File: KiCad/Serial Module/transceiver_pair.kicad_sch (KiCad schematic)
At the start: 22 parts, among them U10 74LVC125, U11 THVD1420D, U12 THVD1420D, U9 74LVC125

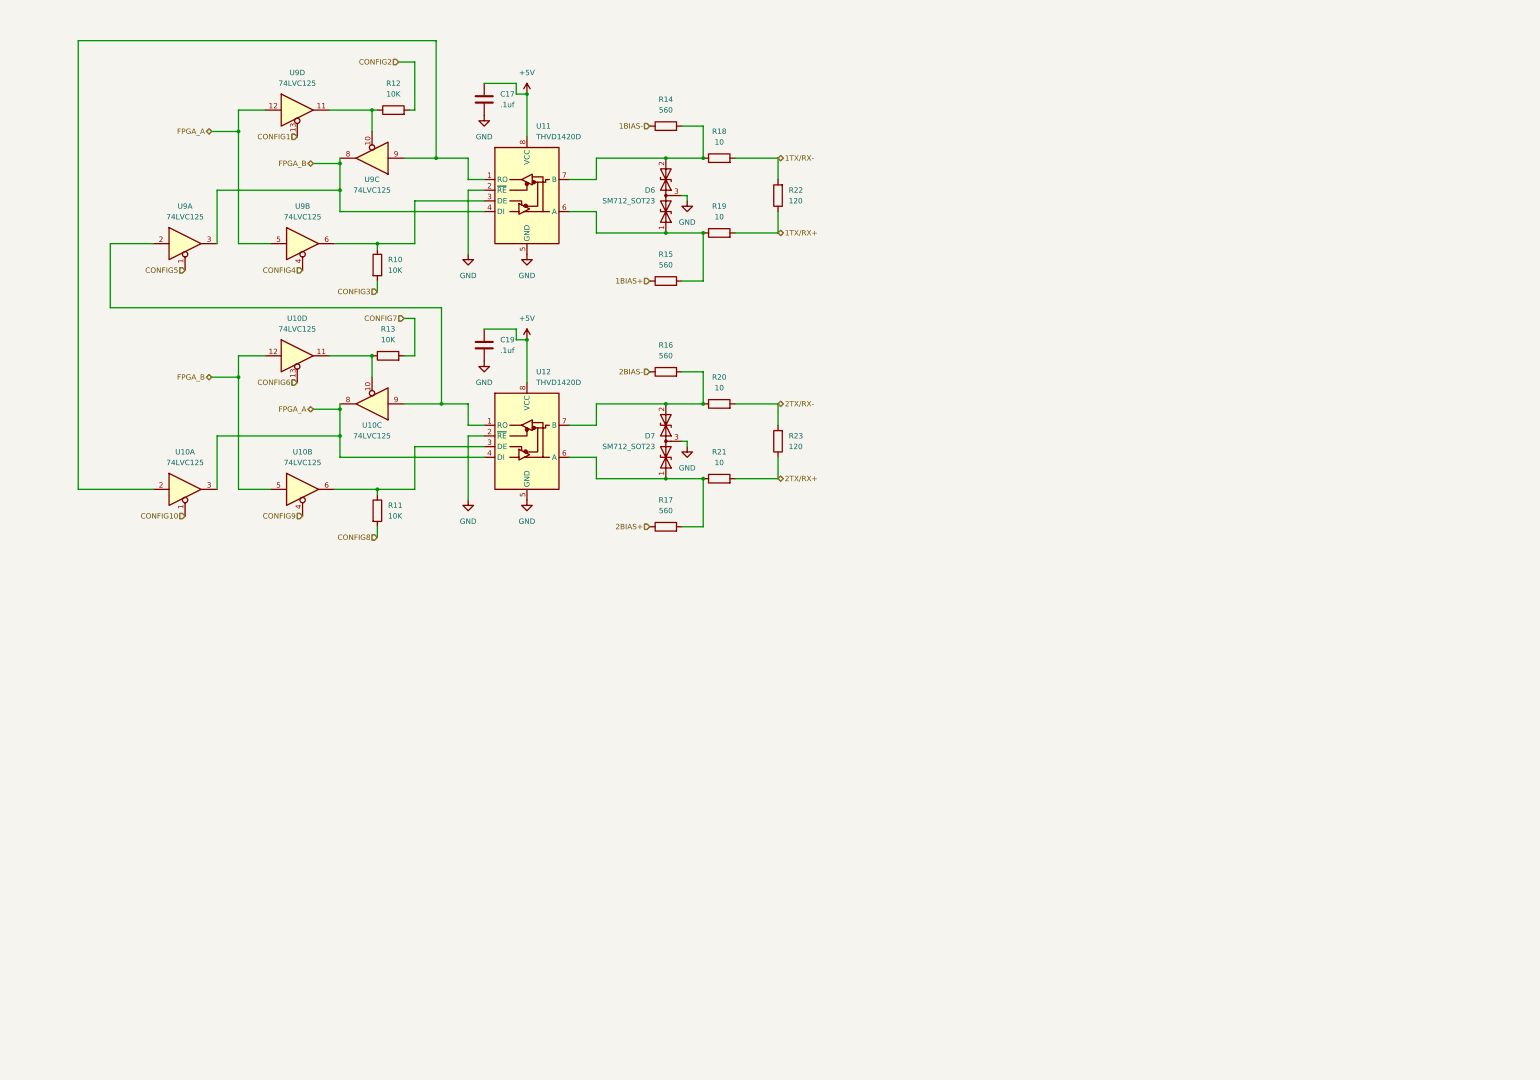
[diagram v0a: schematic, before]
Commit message: update serial module and backplane hw
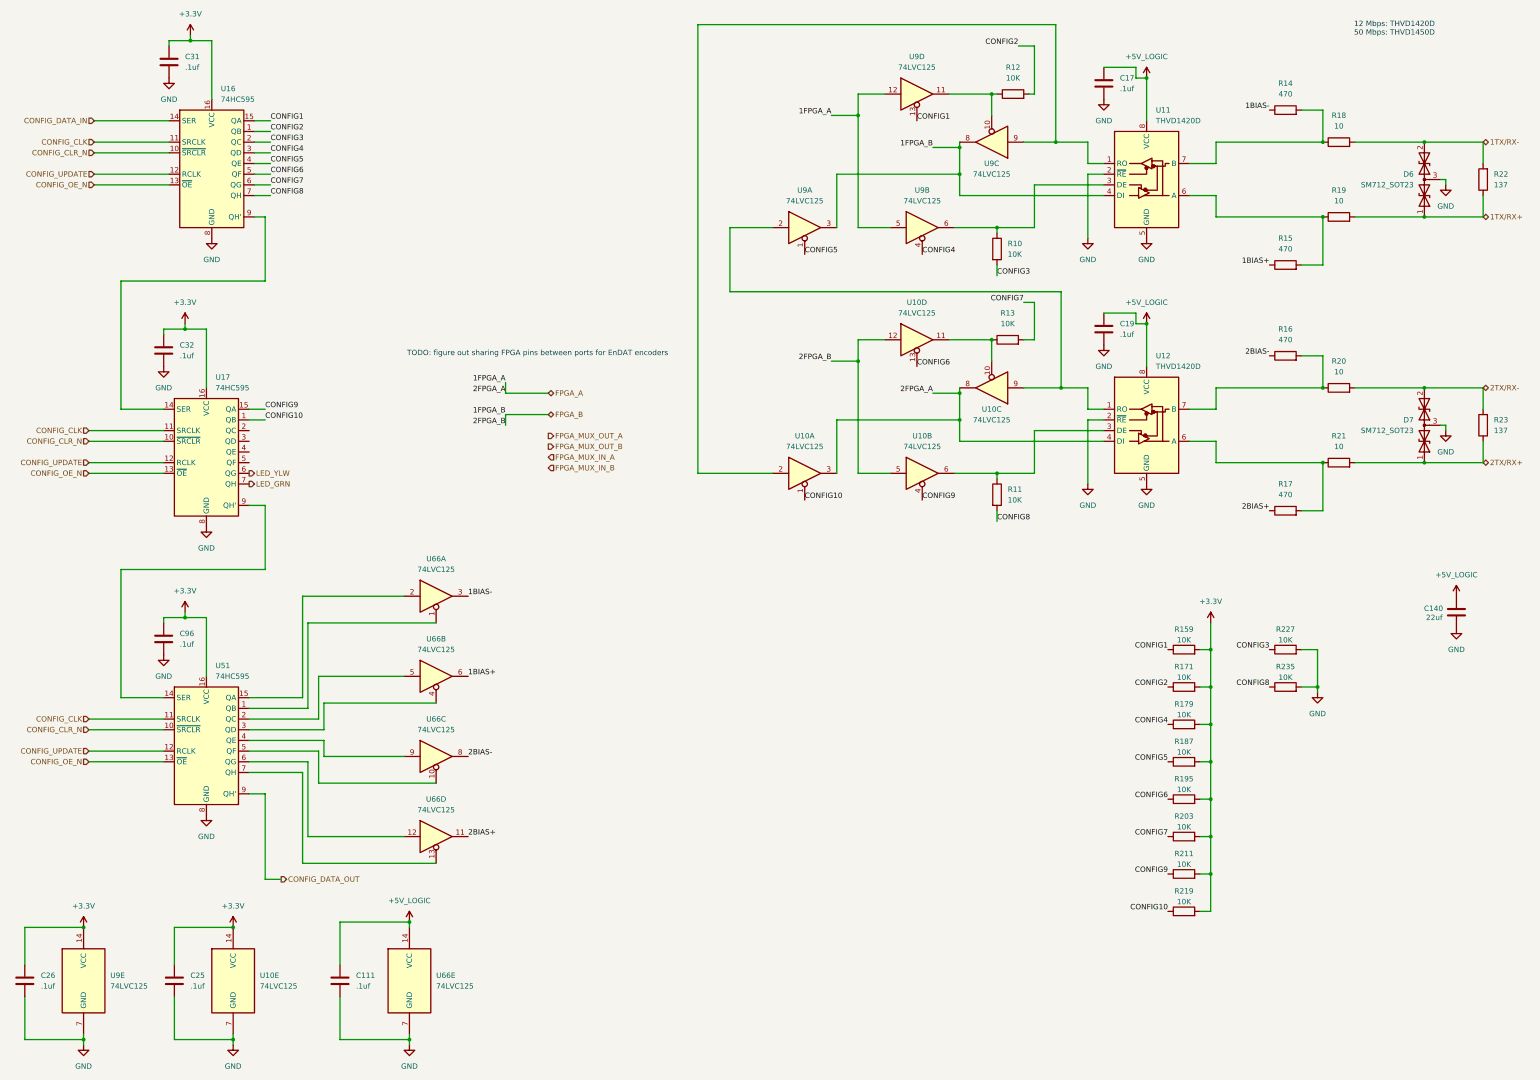
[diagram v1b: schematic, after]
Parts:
- added C111, C25, C26, C31, C32, C96: .1uf, Capacitor_SMD:C_0603_1608Metric, symbol Device:C
- added C140: 22uf, Capacitor_SMD:C_1206_3216Metric, symbol Device:C
- added R159, R171, R179, R187, R195, R203, R211, R219, R227, R235: 10K, Resistor_SMD:R_0603_1608Metric, symbol Device:R
- added unit 5 of U10
- added U16, U17, U51: 74HC595, Package_SO:TSSOP-16_4.4x5mm_P0.65mm, symbol 74xx:74HC595
- added U66: 74LVC125, Package_DFN_QFN:DHVQFN-14-1EP_2.5x3mm_P0.5mm_EP1x1.5mm, symbol 74xx:74LVC125
- added unit 5 of U9
- R14, R15, R16, R17: value 560 -> 470
- R22, R23: value 120 -> 137
- U10, U9: footprint Package_SO:SOIC-14_3.9x8.7mm_P1.27mm -> Package_DFN_QFN:DHVQFN-14-1EP_2.5x3mm_P0.5mm_EP1x1.5mm; LCSC# (none) -> C54411083
- U11, U12: footprint Package_TO_SOT_SMD:SOT-583-8 -> footprints:SOIC-8_4.9x3.91mm_P1.27mm; LCSC# (none) -> C3235215; Manufacturer (none) -> TI; Part Number (none) -> THVD1420DR; cost (none) -> 0.4433
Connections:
- net 1BIAS+: now also U66.6
- net 1BIAS-: now also U66.3
- net 1TX/RX+: now also D6.1 (A1)
- net 1TX/RX-: now also D6.2 (A2)
- net 2BIAS+: now also U66.11
- net 2BIAS-: now also U66.8
- net 2TX/RX+: now also D7.1 (A1)
- net 2TX/RX-: now also D7.2 (A2)
- net CONFIG1: now also R159.1, U16.15 (QA)
- net CONFIG10: now also R219.1, U17.1 (QB)
- net CONFIG2: now also R171.1, U16.1 (QB)
- net CONFIG3: now also R227.1, U16.2 (QC)
- net CONFIG4: now also R179.1, U16.3 (QD)
- net CONFIG5: now also R187.1, U16.4 (QE)
- net CONFIG6: now also R195.1, U16.5 (QF)
- net CONFIG7: now also R203.1, U16.6 (QG)
- net CONFIG8: now also R235.1, U16.7 (QH)
- net CONFIG9: now also R211.1, U17.15 (QA)
- net GND: now also C111.2, C140.1, C25.2, C26.2, C31.2, C32.2, C96.2, R227.2, R235.2, U10.7 (GND), U16.8 (GND), U17.8 (GND), U51.8 (GND), U66.7 (GND), U9.7 (GND)
- net at R14.2, R18.1, U11.7 (B): no longer D6.2 (A2)
- net at R15.2, R19.1, U11.6 (A): no longer D6.1 (A1)
- net at R17.2, R21.1, U12.6 (A): no longer D7.1 (A1)
- net at R16.2, R20.1, U12.7 (B): no longer D7.2 (A2)
- net +5V renamed +5V_LOGIC
- net +5V_LOGIC: now also C111.1, C140.2, U66.14 (VCC)
- new net: U51.5 (QF), U66.10
- new net: U51.4 (QE), U66.9
- new net: U51.3 (QD), U66.4
- new net: U51.2 (QC), U66.5
- new net: U16.9 (QH'), U17.14 (SER)
- new net: U17.9 (QH'), U51.14 (SER)
- new net: U51.6 (QG), U66.12
- new net: U51.7 (QH), U66.13
- new net: U51.1 (QB), U66.1
- new net: U51.15 (QA), U66.2
- new net +3.3V: C25.1, C26.1, C31.1, C32.1, C96.1, R159.2, R171.2, R179.2, R187.2, R195.2, R203.2, R211.2, R219.2, U10.14 (VCC), U16.16 (VCC), U17.16 (VCC), U51.16 (VCC), U9.14 (VCC)
- new net CONFIG_CLK: U16.11 (SRCLK), U17.11 (SRCLK), U51.11 (SRCLK)
- new net CONFIG_CLR_N: U16.10 (~{SRCLR}), U17.10 (~{SRCLR}), U51.10 (~{SRCLR})
- new net CONFIG_DATA_IN: U16.14 (SER)
- new net CONFIG_DATA_OUT: U51.9 (QH')
- new net CONFIG_OE_N: U16.13 (~{OE}), U17.13 (~{OE}), U51.13 (~{OE})
- new net CONFIG_UPDATE: U16.12 (RCLK), U17.12 (RCLK), U51.12 (RCLK)
- new net LED_GRN: U17.7 (QH)
- new net LED_YLW: U17.6 (QG)
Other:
- note added: "12 Mbps: THVD1420D 50 Mbps: THVD1450D"
- note added: "TODO: figure out sharing FPGA pins between ports for EnDAT encoders"
- moved on the sheet: C17, C19, D6, D7, R10, R11, R12, R13, R14, R15, R16, R17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

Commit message: add current limit and sense parts, add possible endat solution
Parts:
- added C159, C167, C175: .1uf, Capacitor_SMD:C_0603_1608Metric, symbol Device:C
- added R289, R297, R305, R313: 10K, Resistor_SMD:R_0603_1608Metric, symbol Device:R
- added U106: 74HC595, Package_SO:TSSOP-16_4.4x5mm_P0.65mm, symbol 74xx:74HC595
- added U28, U90, U98: 74LVC125, Package_DFN_QFN:DHVQFN-14-1EP_2.5x3mm_P0.5mm_EP1x1.5mm, symbol 74xx:74LVC125
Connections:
- net +3.3V: now also C159.1, C167.1, C175.1, R289.2, R297.2, R305.2, R313.2, U106.16 (VCC), U90.14 (VCC), U98.14 (VCC)
- net CONFIG_CLK: now also U106.11 (SRCLK)
- net CONFIG_CLR_N: now also U106.10 (~{SRCLR})
- net CONFIG_OE_N: now also U106.13 (~{OE})
- net CONFIG_UPDATE: now also U106.12 (RCLK)
- net FPGA_A: now also U28.5, U28.9; no longer U12.4 (DI)
- net FPGA_B: now also U28.12, U90.2; no longer U11.4 (DI)
- net GND: now also C159.2, C167.2, C175.2, U106.8 (GND), U90.7 (GND), U98.7 (GND)
- net CONFIG11: now reaches U17.2 (QC)
- net CONFIG11: now also R289.1, U90.1
- net CONFIG12: now reaches U17.3 (QD)
- net CONFIG12: now also R297.1, U28.4
- net CONFIG13: now reaches U17.4 (QE)
- net CONFIG13: now also R305.1, U28.10
- net CONFIG14: now reaches U17.5 (QF)
- net CONFIG14: now also R313.1, U28.13
- net at U17.9 (QH'): now also U106.14 (SER); no longer U51.14 (SER)
- new net: U106.9 (QH'), U51.14 (SER)
- new net CONFIG15: U106.15 (QA), U98.1
- new net CONFIG16: U106.1 (QB), U98.4
- new net CONFIG17: U106.2 (QC), U98.10
- new net CONFIG18: U106.3 (QD), U98.13
- new net DI_A: U11.4 (DI), U90.3, U98.3, U98.6
- new net DI_B: U12.4 (DI), U28.8, U98.11, U98.8
- new net MUX_A: U28.6, U98.2, U98.9
- new net MUX_B: U28.11, U98.12, U98.5
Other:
- note removed: "TODO: figure out sharing FPGA pins between ports for EnDAT encoders"
- moved on the sheet: C111, C31, C32, R10, R11, R12, R13, R227, R235, U10A, U10B, U10C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
